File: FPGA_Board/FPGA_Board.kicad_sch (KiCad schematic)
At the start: 0 parts

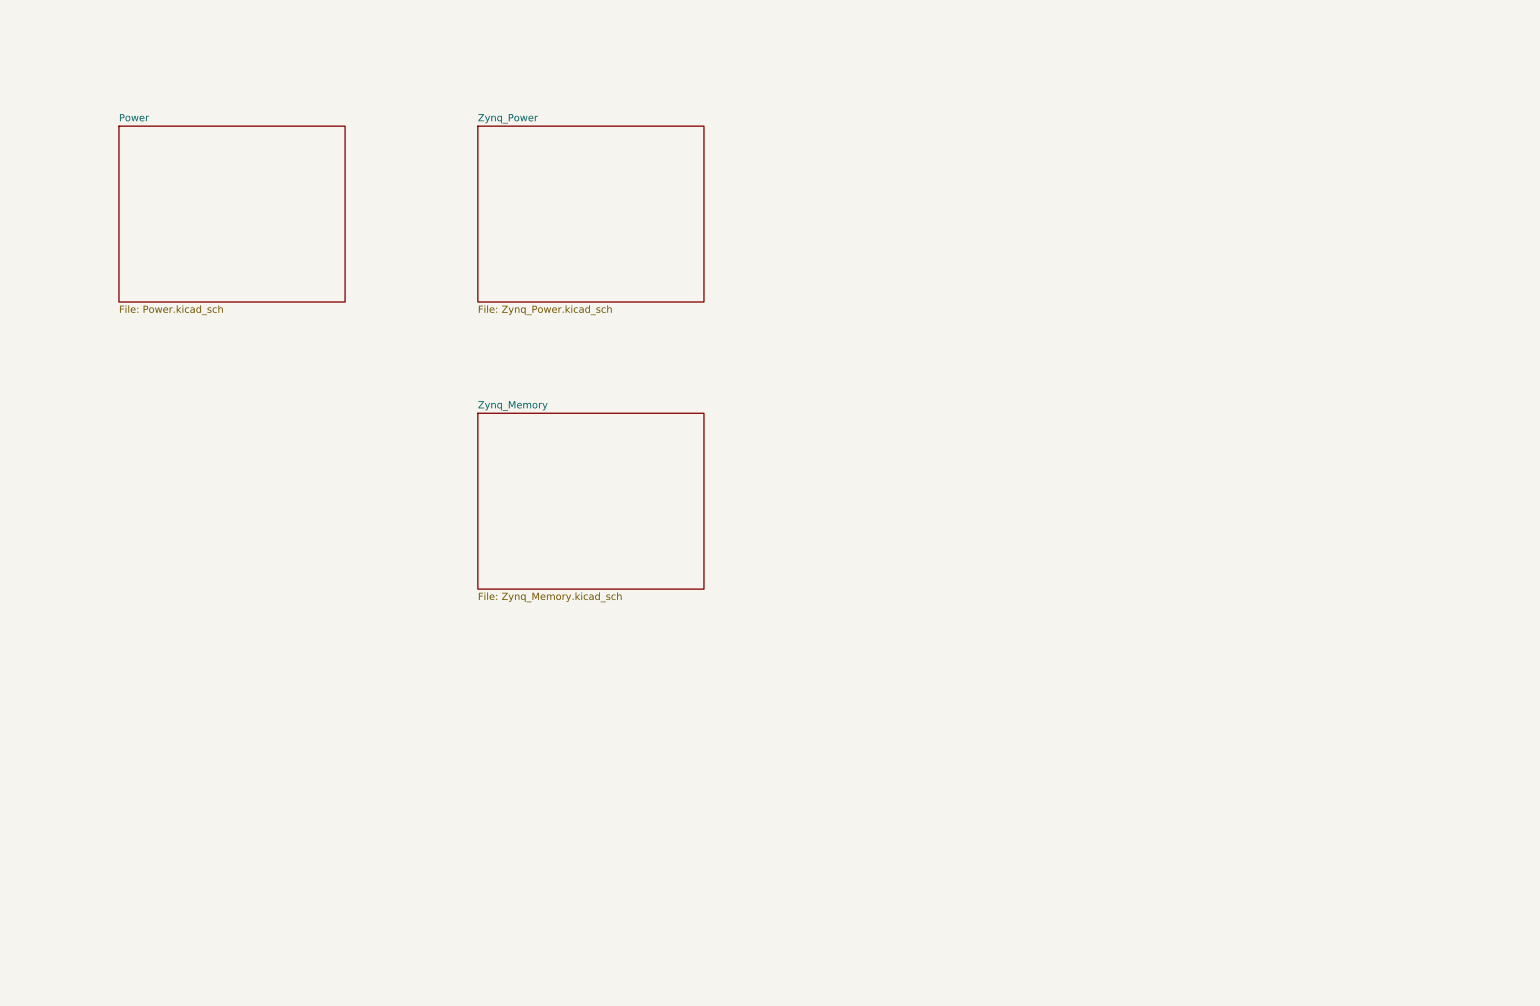
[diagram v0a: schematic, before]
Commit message: Create Block Diagram, create Vivado Project
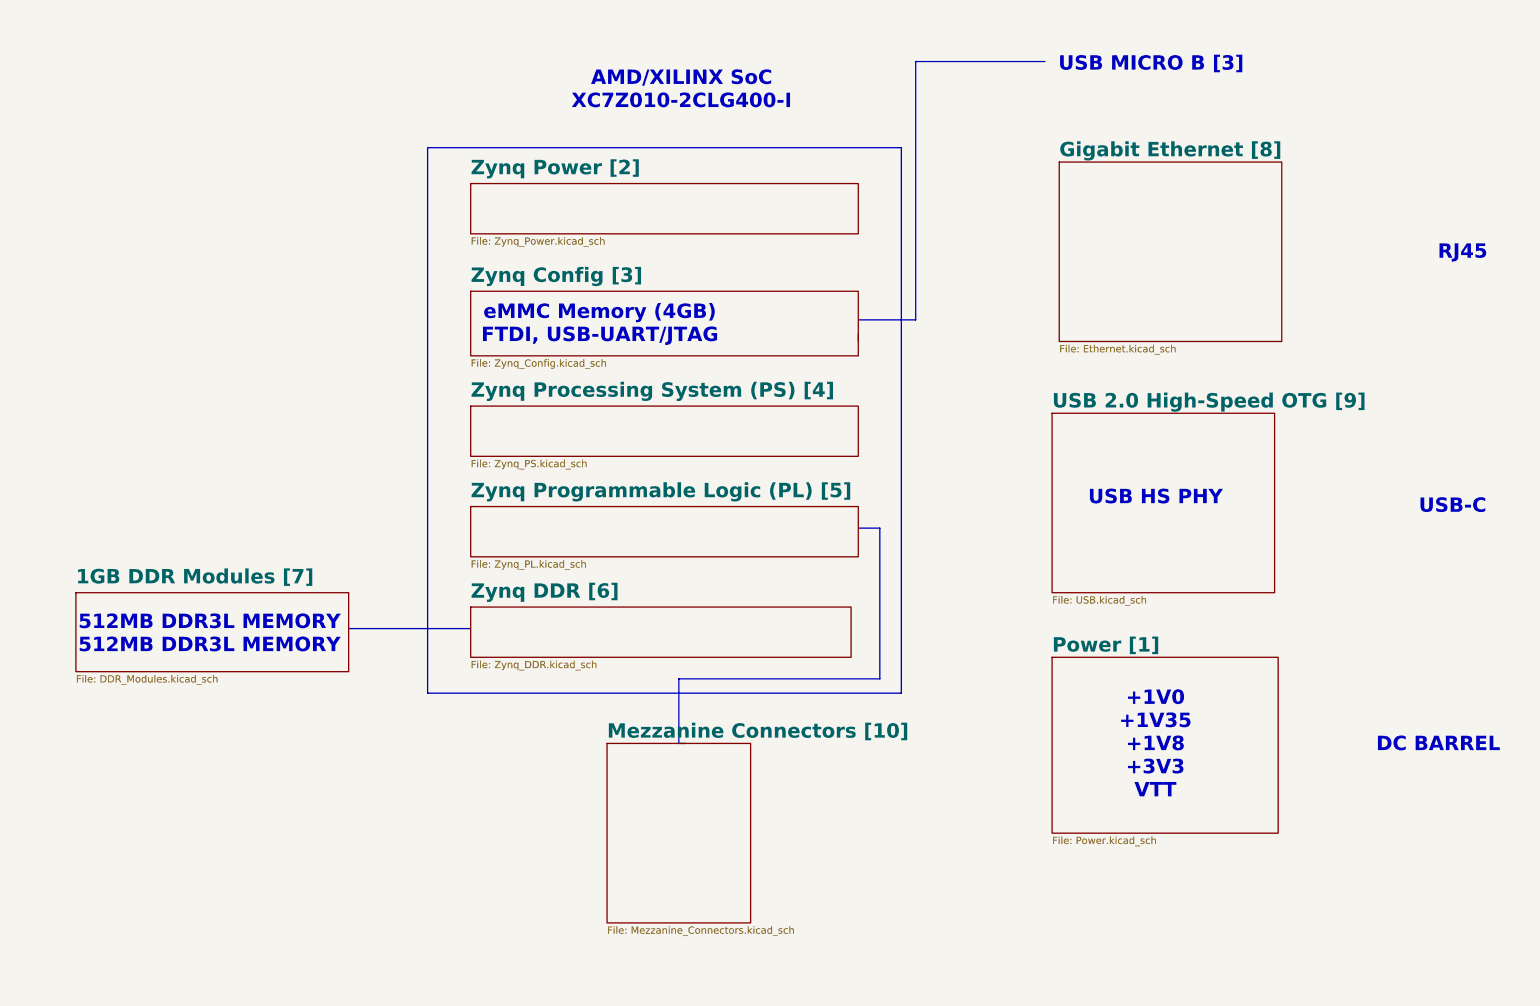
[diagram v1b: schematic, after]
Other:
- sheet Power renamed Power [1]
- removed sheet Zynq_Memory
- removed sheet Zynq_Power
- added sheet 1GB DDR Modules [7] (DDR_Modules.kicad_sch)
- added sheet Gigabit Ethernet [8] (Ethernet.kicad_sch)
- added sheet Mezzanine Connectors [10] (Mezzanine_Connectors.kicad_sch)
- added sheet USB 2.0 High-Speed OTG [9] (USB.kicad_sch)
- added sheet Zynq Config [3] (Zynq_Config.kicad_sch)
- added sheet Zynq DDR [6] (Zynq_DDR.kicad_sch)
- added sheet Zynq Power [2] (Zynq_Power.kicad_sch)
- added sheet Zynq Processing System (PS) [4] (Zynq_PS.kicad_sch)
- added sheet Zynq Programmable Logic (PL) [5] (Zynq_PL.kicad_sch)
- note added: "+1V0 +1V35 +1V8 +3V3 VTT"
- note added: "512MB DDR3L MEMORY 512MB DDR3L MEMORY"
- note added: "AMD/XILINX SoC XC7Z010-2CLG400-I"
- note added: "DC BARREL"
- note added: "RJ45"
- note added: "USB HS PHY"
- note added: "USB MICRO B [3]"
- note added: "USB-C"
- note added: "eMMC Memory (4GB) FTDI, USB-UART/JTAG"

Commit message: - modify USB connector design in FPGA Board
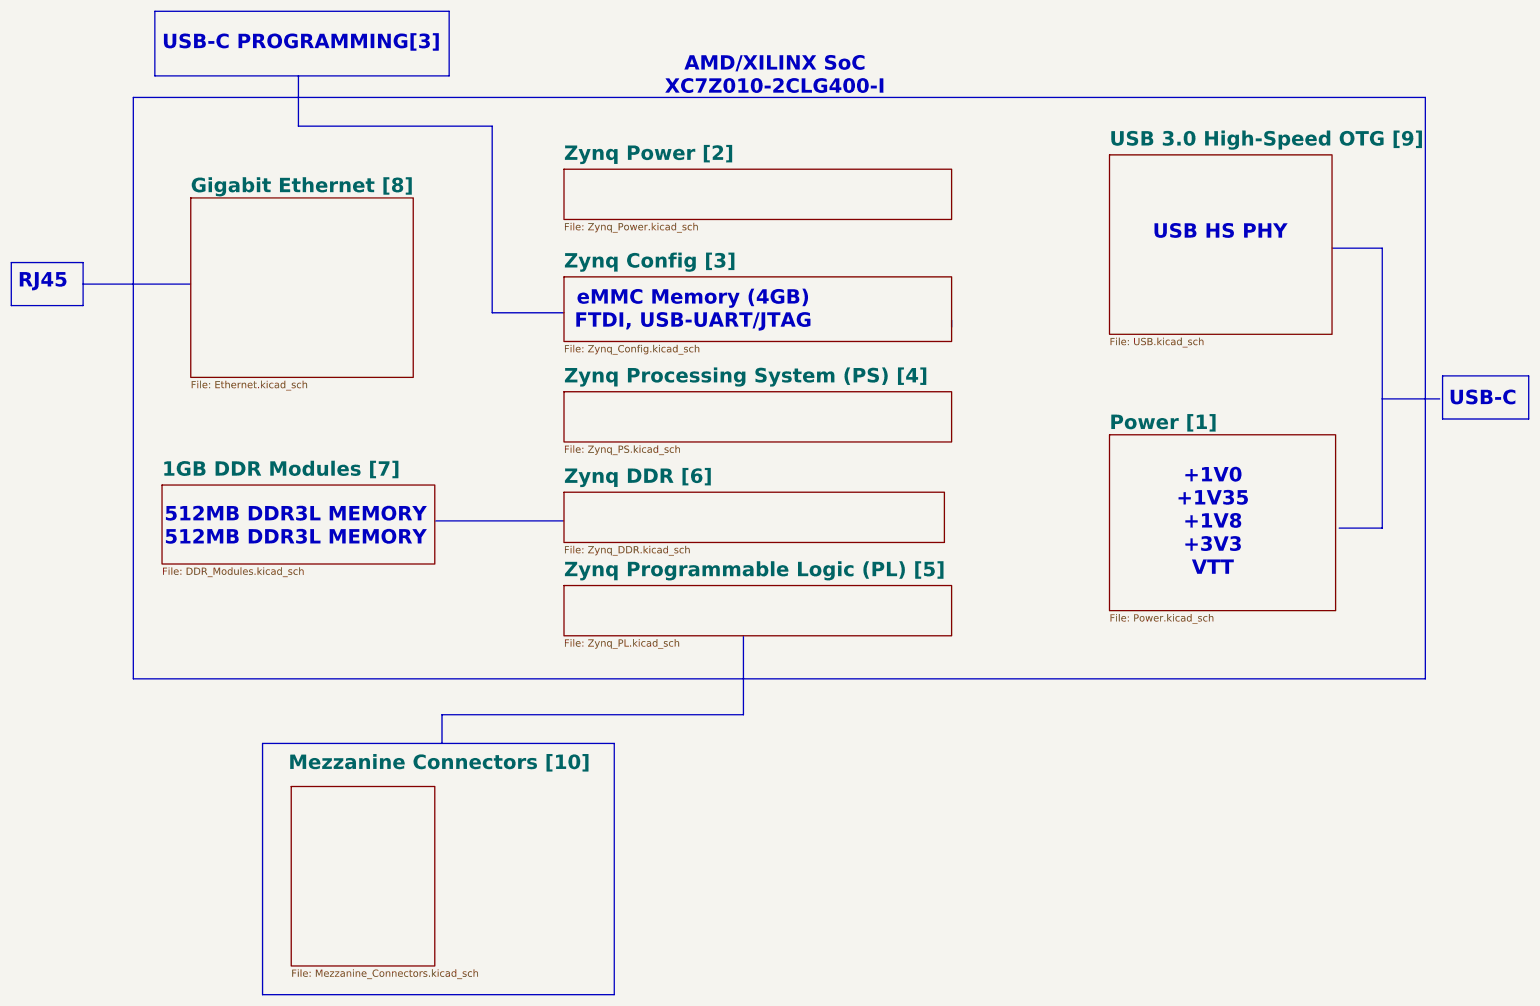
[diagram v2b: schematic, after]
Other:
- sheet USB 2.0 High-Speed OTG [9] renamed USB 3.0 High-Speed OTG [9]
- note added: "USB-C PROGRAMMING[3]"
- note removed: "DC BARREL"
- note removed: "USB MICRO B [3]"

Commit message: fix 'USB 3.0' typo, add USB C connector and eFuse
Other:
- sheet USB 3.0 High-Speed OTG [9] renamed USB 2.0 High-Speed OTG [9]
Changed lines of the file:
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@@
 			(color 0 0 0 0)
 		)
-		(property "Sheetname" "USB 3.0 High-Speed OTG [9]"
+		(property "Sheetname" "USB 2.0 High-Speed OTG [9]"
 			(at 209.55 39.2934 0)
 			(show_name no)
